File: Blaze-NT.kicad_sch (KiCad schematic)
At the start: 0 parts

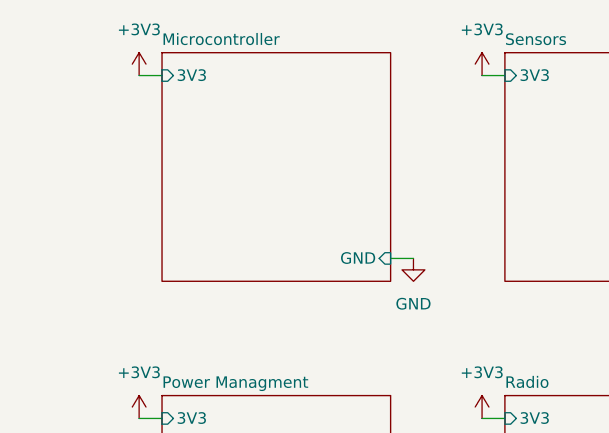
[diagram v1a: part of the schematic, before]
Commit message: Microcontroller topsheet
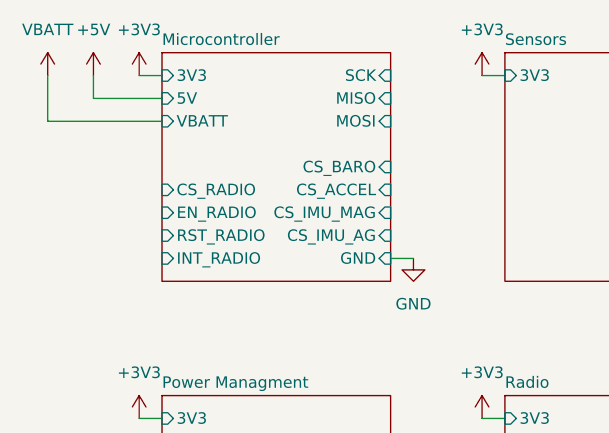
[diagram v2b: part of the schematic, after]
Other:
- sheet Microcontroller ports: added 5V, CS_ACCEL, CS_BARO, CS_IMU_AG, CS_IMU_MAG, CS_RADIO, EN_RADIO, INT_RADIO, MISO, MOSI, RST_RADIO, SCK, VBATT; removed none

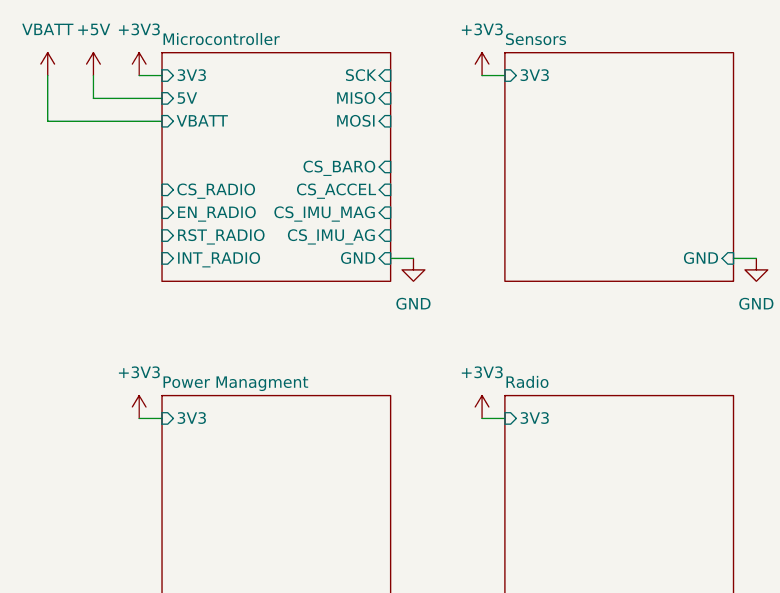
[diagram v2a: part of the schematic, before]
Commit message: Updated heiarchal power labels
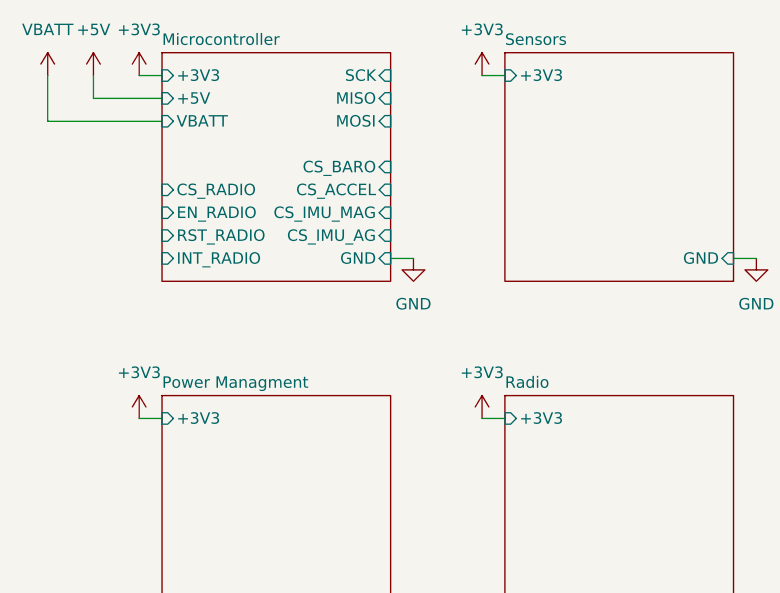
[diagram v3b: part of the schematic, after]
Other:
- sheet Microcontroller ports: added +3V3, +5V; removed 3V3, 5V
- sheet Power Managment ports: added +3V3; removed 3V3
- sheet Radio ports: added +3V3; removed 3V3
- sheet Sensors ports: added +3V3; removed 3V3
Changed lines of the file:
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@@
-			)
-		)
-		(pin "3V3" input
-			(at 114.3 66.04 180)
-			(effects
-				(font
-					(size 1.27 1.27)
-				)
-				(justify left)
 			)
 		)
@@
 			)
 		)
-		(pin "5V" input
-			(at 114.3 68.58 180)
-			(effects
-				(font
-					(size 1.27 1.27)
-				)
-				(justify left)
-			)
-		)
 		(pin "CS_RADIO" input
 			(at 114.3 78.74 180)
@@
 		(pin "VBATT" input
 			(at 114.3 71.12 180)
+			(effects
+				(font
+					(size 1.27 1.27)
+				)
+				(justify left)
+			)
+		)
+		(pin "+5V" input
+			(at 114.3 68.58 180)
+			(effects
+				(font
+					(size 1.27 1.27)
+				)
+				(justify left)
+			)
+		)
+		(pin "+3V3" input
+			(at 114.3 66.04 180)
 			(effects
 				(font
@@
 			)
 		)
-		(pin "3V3" input
+		(pin "+3V3" input
 			(at 152.4 104.14 180)
 			(effects
@@
 			)
 		)
-		(pin "3V3" input
+		(pin "+3V3" input
 			(at 152.4 66.04 180)
 			(effects
@@
 			)
 		)
-		(pin "3V3" input
-			(at 114.3 104.14 180)
-			(effects
-				(font
-					(size 1.27 1.27)
-				)
-				(justify left)
-			)
-		)
 		(pin "GND" input
 			(at 139.7 124.46 0)
@@
 			)
 		)
+		(pin "+3V3" input
+			(at 114.3 104.14 180)
+			(effects
+				(font
+					(size 1.27 1.27)
+				)
+				(justify left)
+			)
+		)

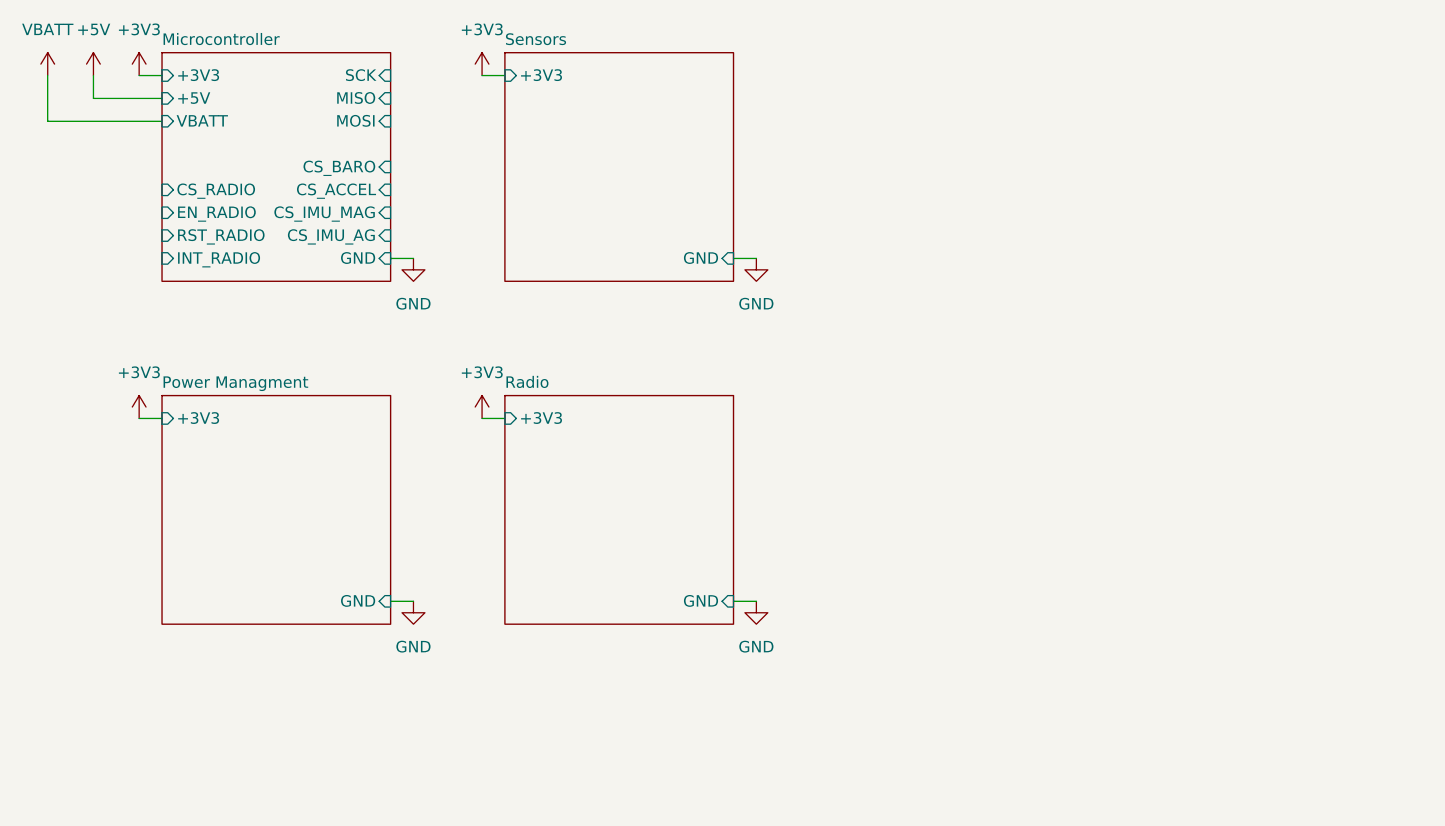
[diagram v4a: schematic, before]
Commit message: Connected topsheet
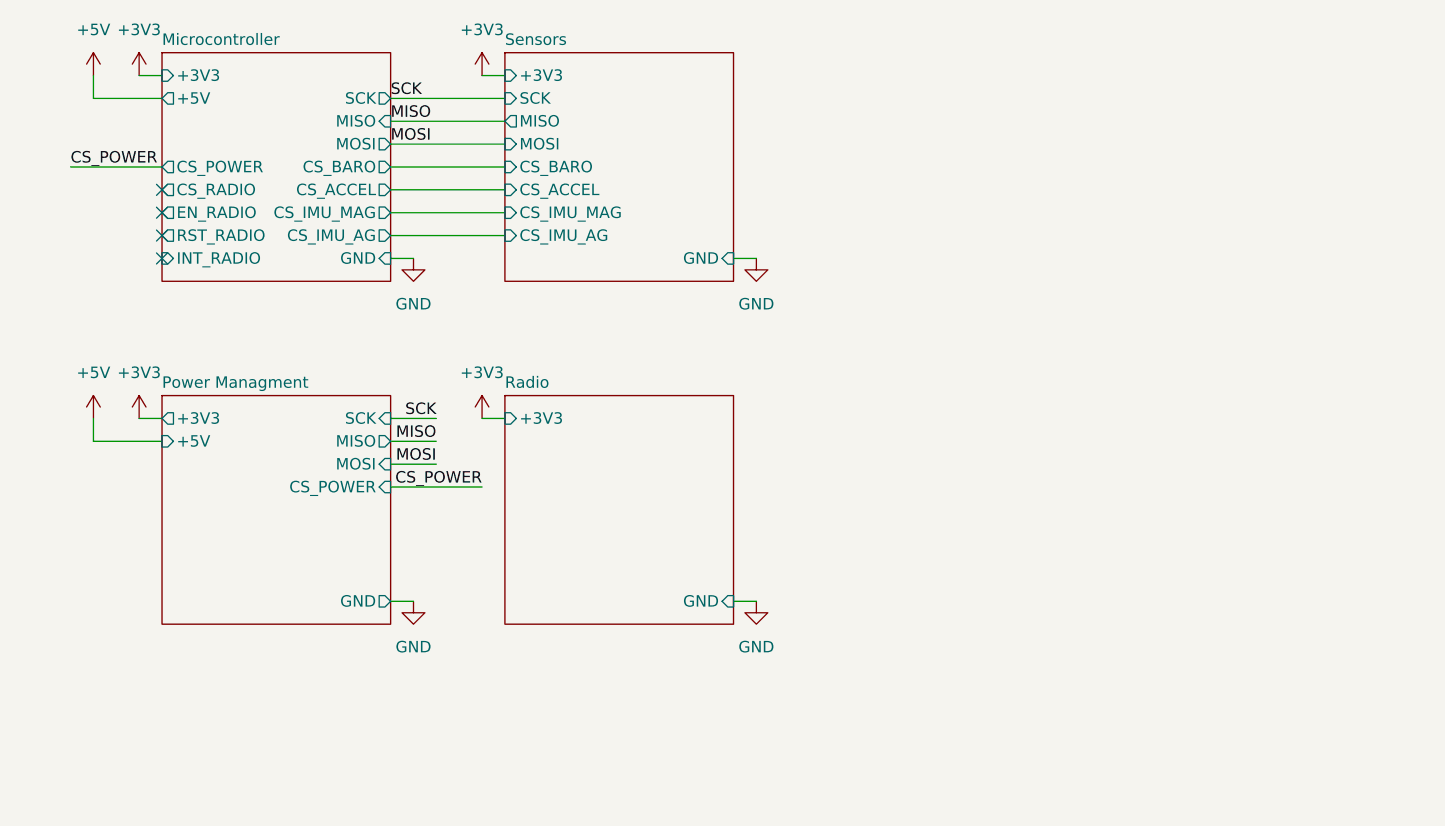
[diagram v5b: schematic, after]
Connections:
- no-connect marks 0 -> 4
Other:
- sheet Microcontroller ports: added CS_POWER; removed VBATT
- sheet Power Managment ports: added +5V, CS_POWER, MISO, MOSI, SCK; removed none
- sheet Sensors ports: added CS_ACCEL, CS_BARO, CS_IMU_AG, CS_IMU_MAG, MISO, MOSI, SCK; removed none

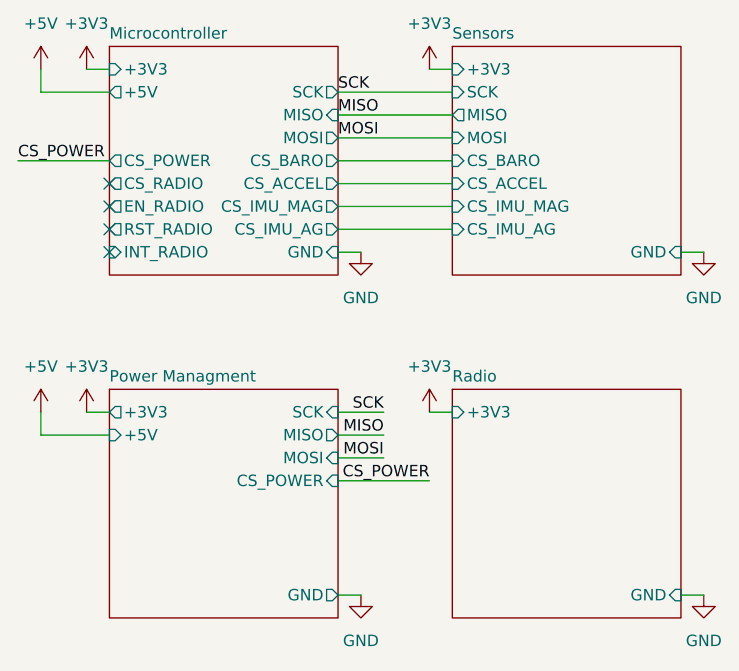
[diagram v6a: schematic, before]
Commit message: Connected radio
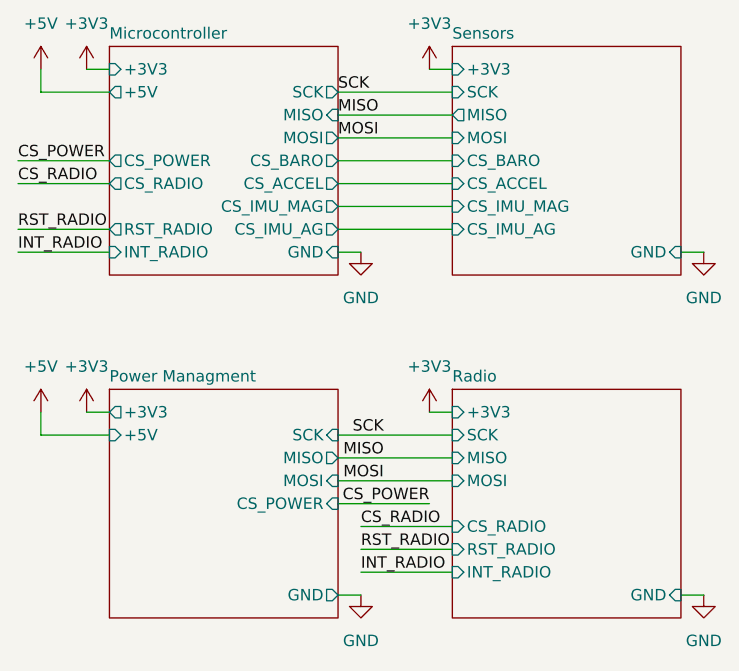
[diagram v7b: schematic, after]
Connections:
- no-connect marks 4 -> 0
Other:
- sheet Microcontroller ports: added none; removed EN_RADIO
- sheet Radio ports: added CS_RADIO, INT_RADIO, MISO, MOSI, RST_RADIO, SCK; removed none
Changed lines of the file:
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@@
 		(company "UCSC Rocket Team")
 	)
-	(no_connect
-		(at 114.3 81.28)
-	)
-	(no_connect
-		(at 114.3 83.82)
-	)
-	(no_connect
-		(at 114.3 78.74)
-	)
-	(no_connect
-		(at 114.3 86.36)
-	)
 	(wire
 		(pts
@@
 	(wire
 		(pts
+			(xy 142.24 119.38) (xy 152.4 119.38)
+		)
+		(stroke
+			(width 0)
+			(type default)
+		)
+	)
+	(wire
+		(pts
+			(xy 104.14 83.82) (xy 114.3 83.82)
+		)
+		(stroke
+			(width 0)
+			(type default)
+		)
+	)
+	(wire
+		(pts
 			(xy 139.7 86.36) (xy 142.24 86.36)
 		)
@@
 	(wire
 		(pts
-			(xy 144.78 106.68) (xy 139.7 106.68)
+			(xy 139.7 109.22) (xy 152.4 109.22)
 		)
 		(stroke
@@
 	(wire
 		(pts
+			(xy 142.24 121.92) (xy 152.4 121.92)
+		)
+		(stroke
+			(width 0)
+			(type default)
+		)
+	)
+	(wire
+		(pts
 			(xy 139.7 83.82) (xy 152.4 83.82)
 		)
@@
 	(wire
 		(pts
+			(xy 142.24 116.84) (xy 152.4 116.84)
+		)
+		(stroke
+			(width 0)
+			(type default)
+		)
+	)
+	(wire
+		(pts
 			(xy 177.8 124.46) (xy 180.34 124.46)
 		)
@@
 	(wire
 		(pts
-			(xy 144.78 109.22) (xy 139.7 109.22)
-		)
-		(stroke
-			(width 0)
-			(type default)
-		)
-	)
-	(wire
-		(pts
-			(xy 144.78 104.14) (xy 139.7 104.14)
+			(xy 139.7 111.76) (xy 152.4 111.76)
+		)
+		(stroke
+			(width 0)
+			(type default)
+		)
+	)
+	(wire
+		(pts
+			(xy 104.14 78.74) (xy 114.3 78.74)
+		)
+		(stroke
+			(width 0)
+			(type default)
+		)
+	)
+	(wire
+		(pts
+			(xy 139.7 106.68) (xy 152.4 106.68)
 		)
 		(stroke
@@
 	(wire
 		(pts
-			(xy 149.86 111.76) (xy 139.7 111.76)
+			(xy 149.86 114.3) (xy 139.7 114.3)
 		)
 		(stroke
@@
 	(wire
 		(pts
+			(xy 104.14 86.36) (xy 114.3 86.36)
+		)
+		(stroke
+			(width 0)
+			(type default)
+		)
+	)
+	(wire
+		(pts
 			(xy 139.7 124.46) (xy 142.24 124.46)
 		)
@@
 	)
 	(label "MISO"
-		(at 144.78 106.68 180)
+		(at 144.78 109.22 180)
 		(effects
 			(font
@@
 		)
 	)
+	(label "INT_RADIO"
+		(at 104.14 86.36 0)
+		(effects
+			(font
+				(size 1.27 1.27)
+			)
+			(justify left bottom)
+		)
+	)
+	(label "RST_RADIO"
+		(at 142.24 119.38 0)
+		(effects
+			(font
+				(size 1.27 1.27)
+			)
+			(justify left bottom)
+		)
+	)
+	(label "CS_RADIO"
+		(at 142.24 116.84 0)
+		(effects
+			(font
+				(size 1.27 1.27)
+			)
+			(justify left bottom)
+		)
+	)
 	(label "CS_POWER"
 		(at 104.14 76.2 0)
@@
 	)
 	(label "CS_POWER"
-		(at 149.86 111.76 180)
+		(at 149.86 114.3 180)
 		(effects
 			(font
@@
 		)
 	)
-	(label "MOSI"
-		(at 144.78 109.22 180)
+	(label "INT_RADIO"
+		(at 142.24 121.92 0)
 		(effects
 			(font
 				(size 1.27 1.27)
 			)
+			(justify left bottom)
+		)
+	)
+	(label "MOSI"
+		(at 144.78 111.76 180)
+		(effects
+			(font
+				(size 1.27 1.27)
+			)
 			(justify right bottom)
 		)
 	)
+	(label "CS_RADIO"
+		(at 104.14 78.74 0)
+		(effects
+			(font
+				(size 1.27 1.27)
+			)
+			(justify left bottom)
+		)
+	)
 	(label "SCK"
-		(at 144.78 104.14 180)
+		(at 144.78 106.68 180)
 		(effects
 			(font
@@
 	(label "MISO"
 		(at 139.7 71.12 0)
+		(effects
+			(font
+				(size 1.27 1.27)
+			)
+			(justify left bottom)
+		)
+	)
+	(label "RST_RADIO"
+		(at 104.14 83.82 0)
 		(effects
 			(font
@@
 			)
 		)
-		(pin "EN_RADIO" output
-			(at 114.3 81.28 180)
-			(effects
-				(font
-					(size 1.27 1.27)
-				)
-				(justify left)
-			)
-		)
 		(pin "RST_RADIO" output
 			(at 114.3 83.82 180)
@@
 			)
 		)
+		(pin "MOSI" input
+			(at 152.4 111.76 180)
+			(effects
+				(font
+					(size 1.27 1.27)
+				)
+				(justify left)
+			)
+		)
+		(pin "CS_RADIO" input
+			(at 152.4 116.84 180)
+			(effects
+				(font
+					(size 1.27 1.27)
+				)
+				(justify left)
+			)
+		)
+		(pin "RST_RADIO" input
+			(at 152.4 119.38 180)
+			(effects
+				(font
+					(size 1.27 1.27)
+				)
+				(justify left)
+			)
+		)
+		(pin "MISO" input
+			(at 152.4 109.22 180)
+			(effects
+				(font
+					(size 1.27 1.27)
+				)
+				(justify left)
+			)
+		)
+		(pin "SCK" input
+			(at 152.4 106.68 180)
+			(effects
+				(font
+					(size 1.27 1.27)
+				)
+				(justify left)
+			)
+		)
+		(pin "INT_RADIO" input
+			(at 152.4 121.92 180)
+			(effects
+				(font
+					(size 1.27 1.27)
+				)
+				(justify left)
+			)
+		)
 		(instances
 			(project "Blaze-NT"
@@
 		)
 		(pin "MOSI" input
-			(at 139.7 109.22 0)
+			(at 139.7 111.76 0)
 			(effects
 				(font
@@
 		)
 		(pin "MISO" output
-			(at 139.7 106.68 0)
+			(at 139.7 109.22 0)
 			(effects
 				(font
@@
 		)
 		(pin "CS_POWER" input
-			(at 139.7 111.76 0)
+			(at 139.7 114.3 0)
 			(effects
 				(font
@@
 		)
 		(pin "SCK" input
-			(at 139.7 104.14 0)
-			(effects
-				(font
+			(at 139.7 106.68 0)
+			(effects
+				(font

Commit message: PCB work
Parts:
- added H1, H2, H3, H4: MP, MountingHole:MountingHole_3.2mm_M3_ISO7380_Pad, symbol Mechanical:MountingHole_Pad
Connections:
- net GND: now also H1.1, H2.1, H3.1, H4.1
